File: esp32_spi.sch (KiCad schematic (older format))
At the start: 15 parts

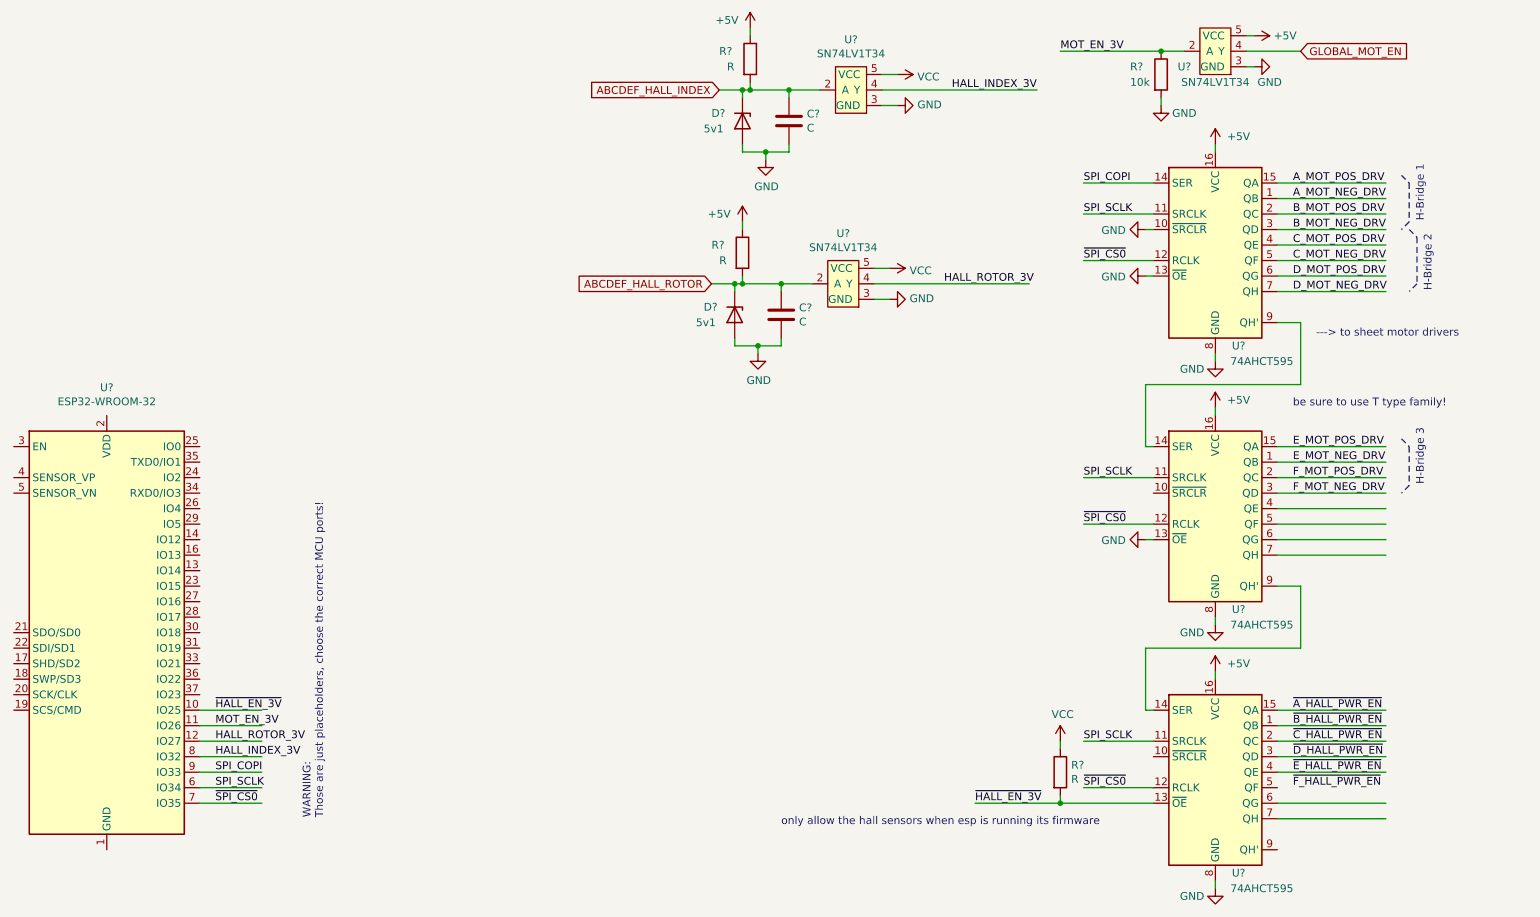
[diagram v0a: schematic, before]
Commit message: Added footprints.
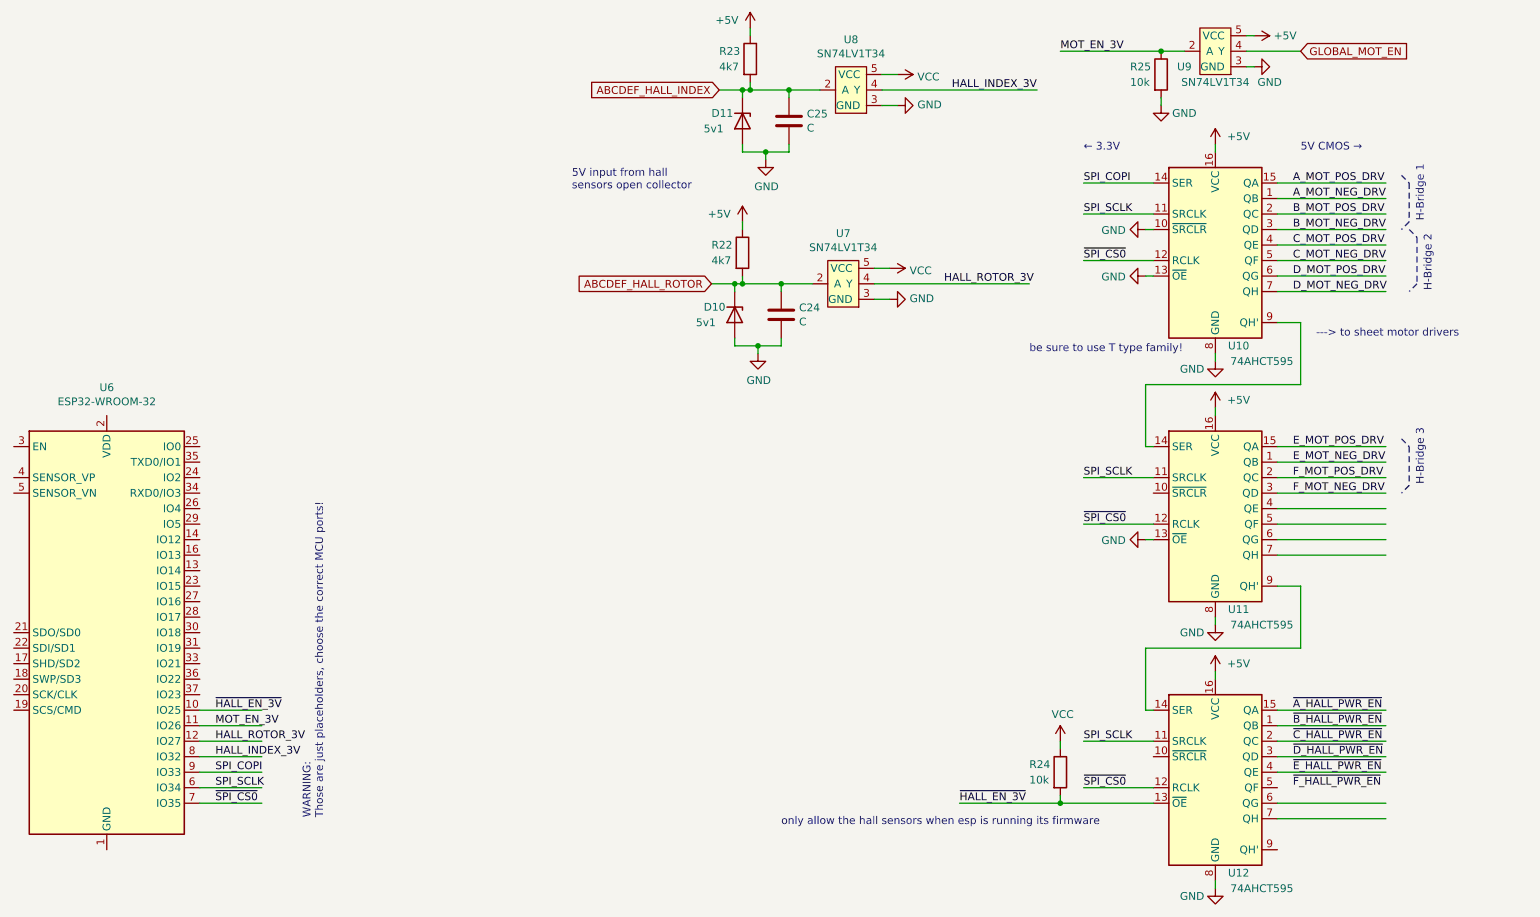
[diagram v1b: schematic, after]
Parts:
- C24, C25: renamed from C?; footprint (none) -> Capacitor_SMD:C_0603_1608Metric
- D10, D11: renamed from D?; footprint (none) -> Diode_SMD:D_SMB_Handsoldering
- R22, R23: renamed from R?; value R -> 4k7; footprint (none) -> Resistor_SMD:R_0603_1608Metric
- R24: renamed from R?; value R -> 10k; footprint (none) -> Resistor_SMD:R_0603_1608Metric
- R25: renamed from R?; footprint (none) -> Resistor_SMD:R_0603_1608Metric
- U10, U11, U12: renamed from U?; footprint (none) -> Package_SO:SOIC-16_3.9x9.9mm_P1.27mm
- gave numbers to parts that had none: 4
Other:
- note added: "5V CMOS →"
- note added: "5V input from hall\nsensors open collector"
- note added: "← 3.3V"
